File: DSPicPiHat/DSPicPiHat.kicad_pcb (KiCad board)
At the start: 2 copper layers, 65 x 66.5 mm, 87 parts, among them J10 Nice!View, J4 Conn_PIC_ICSP_ICD, J5 USB_C_Receptacle_USB2.0, J6 PowerInput, J7 GenericSPIconn, J8 RasPiHeaders, J9 GeneralSPIDisplay, SW1 POWER_Select, SW2 SW_DIP_x08, U1 DSPIC33CH512MP508T-I_PT, U10 DF5A6.2CJE_LM, U11 FT230XS, U12 NCP1117-3.3_SOT223, U2 ISO1640BDR, U3 DF5A6.2CJE_LM, U4 DF5A6.2CJE_LM, U5 ISO1640BDR, U6 DF5A6.2CJE_LM, U7 DF5A6.2CJE_LM, U8 ISO1640BDR, U9 DF5A6.2CJE_LM

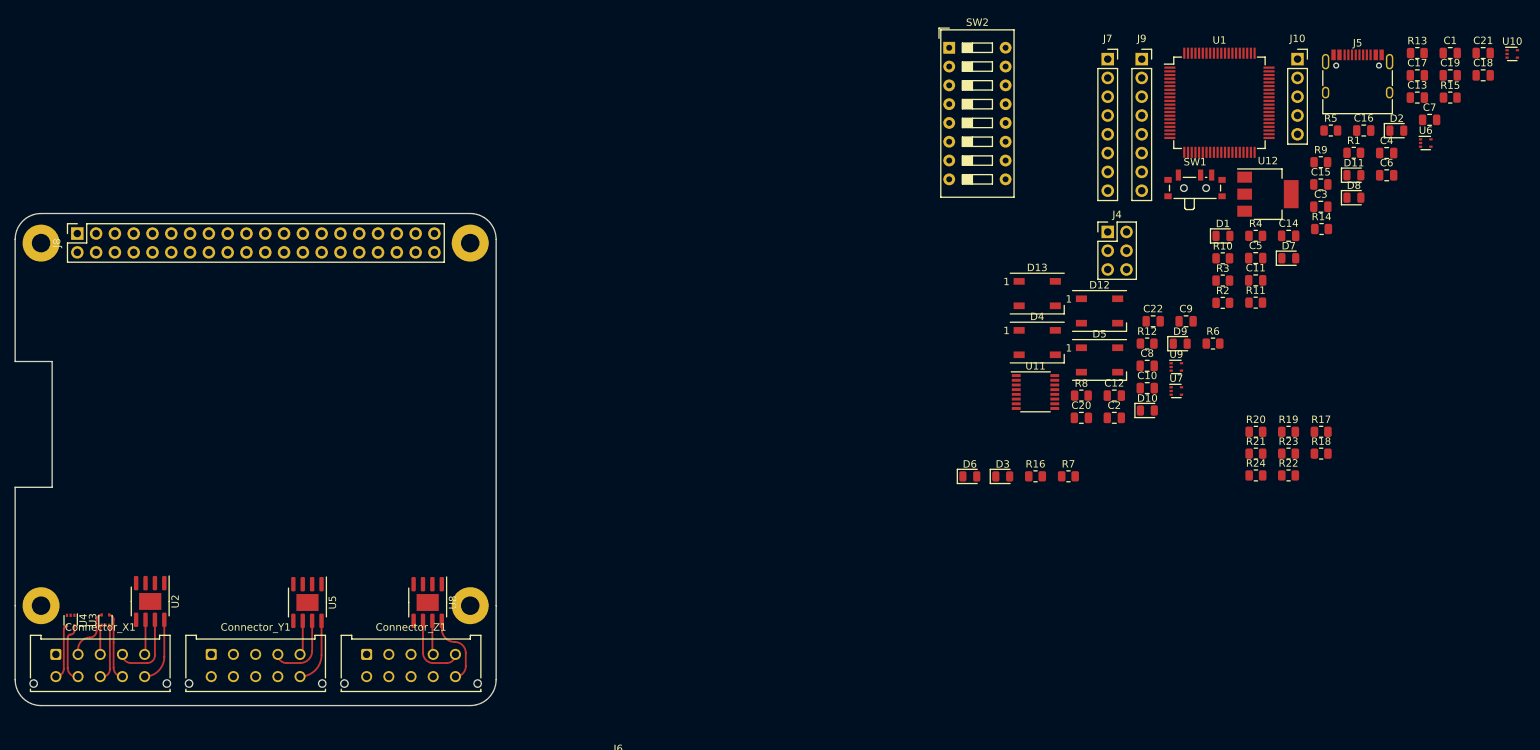
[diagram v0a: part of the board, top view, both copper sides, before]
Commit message: ESD connected to axis connectors.
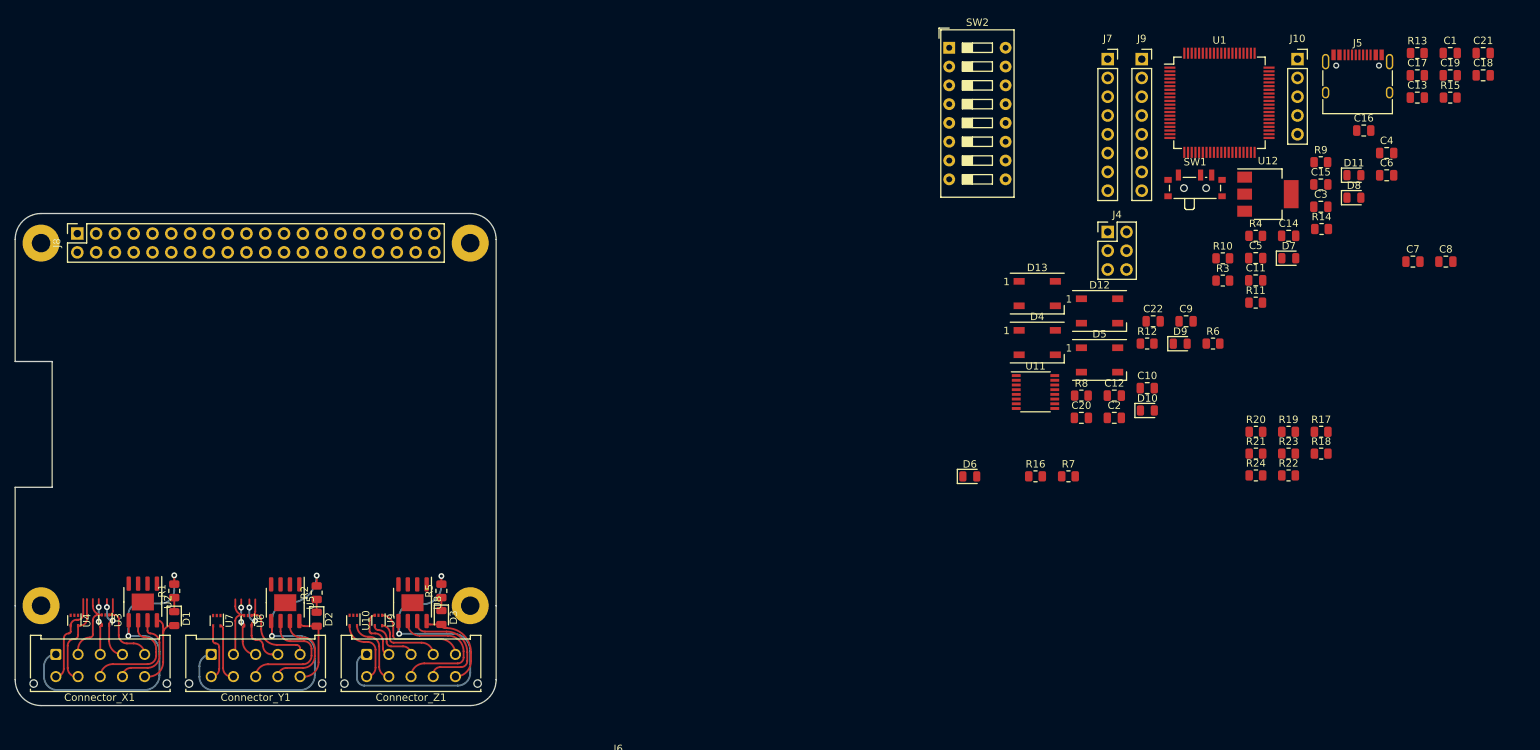
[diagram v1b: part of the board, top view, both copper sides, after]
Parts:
- moved U10 174.3 mm to (102.2, 128.5), turned to -90 degrees
- moved U6 171.8 mm to (88.0, 128.5), turned to -90 degrees
- moved R1 170.0 mm to (78.0, 124.5), turned to 90 degrees
- moved D2 160.2 mm to (97.2, 128.3), turned to -90 degrees
- moved D1 150.9 mm to (78.0, 128.2), turned to -90 degrees
- moved R5 135.3 mm to (114.1, 124.5), turned to 90 degrees
- moved U7 133.3 mm to (83.8, 128.5), turned to -90 degrees
- moved R2 128.6 mm to (97.2, 124.7), turned to 90 degrees
- moved U9 113.1 mm to (105.6, 128.5), turned to -90 degrees
- moved D3 78.2 mm to (114.1, 128.1), turned to -90 degrees
- moved C8 42.8 mm to (249.8, 80.0)
- moved C7 19.3 mm to (245.4, 80.0)
- moved U5 3.00 mm to (93.0, 126.1)
- moved U8 2.05 mm to (110.2, 126.1)
- moved U2 1.00 mm to (73.8, 126.0)
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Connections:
- Connector_X1 pad 2: EXT_X_PWM_00 -> EXT_ADC_X_00
- Connector_X1 pad 3: EXT_X_PWM_01 -> EXT_ADC_X_01
- Connector_X1 pad 4: EXT_X_SDA -> EXT_ADC_X_02
- Connector_X1 pad 5: EXT_X_SCL -> EXT_ADC_X_03
- Connector_X1 pad 6: EXT_ADC_X_00 -> EXT_X_PWM_00
- Connector_X1 pad 7: EXT_ADC_X_01 -> EXT_X_PWM_01
- Connector_X1 pad 8: EXT_ADC_X_02 -> EXT_X_SCL
- Connector_X1 pad 9: EXT_ADC_X_03 -> EXT_X_SDA
- Connector_Y1 pad 1: GNDY -> GNDZ
- Connector_Y1 pad 2: EXT_Y_PWM_00 -> EXT_ADC_Y_00
- Connector_Y1 pad 3: EXT_Y_PWM_01 -> EXT_ADC_Y_01
- Connector_Y1 pad 4: EXT_Y_SDA -> EXT_ADC_Y_02
- Connector_Y1 pad 5: EXT_Y_SCL -> EXT_ADC_Y_03
- Connector_Y1 pad 6: EXT_ADC_Y_00 -> EXT_Y_PWM_00
- Connector_Y1 pad 7: EXT_ADC_Y_01 -> EXT_Y_PWM_01
- Connector_Y1 pad 8: EXT_ADC_Y_02 -> EXT_Y_SCL
- Connector_Y1 pad 9: EXT_ADC_Y_03 -> EXT_Y_SDA
- Connector_Z1 pad 2: EXT_Z_PWM_00 -> EXT_ADC_Z_00
- Connector_Z1 pad 3: EXT_Z_PWM_01 -> EXT_ADC_Z_01
- Connector_Z1 pad 4: EXT_Z_SDA -> EXT_ADC_Z_02
- Connector_Z1 pad 5: EXT_Z_SCL -> EXT_ADC_Z_03
- Connector_Z1 pad 6: EXT_ADC_Z_00 -> EXT_Z_PWM_00
- Connector_Z1 pad 7: EXT_ADC_Z_01 -> EXT_Z_PWM_01
- Connector_Z1 pad 8: EXT_ADC_Z_02 -> EXT_Z_SCL
- Connector_Z1 pad 9: EXT_ADC_Z_03 -> EXT_Z_SDA
- U10 pad 3: EXT_Z_PWM_01 -> unconnected-(U10-Pad3)
- U10 pad 4: unconnected-(U10-Pad4) -> EXT_Z_PWM_00
- U10 pad 5: unconnected-(U10-Pad5) -> EXT_Z_PWM_01
- U3 pad 1: EXT_X_PWM_01 -> EXT_ADC_X_03
- U3 pad 3: EXT_ADC_X_02 -> EXT_ADC_X_00
- U3 pad 4: EXT_ADC_X_03 -> EXT_ADC_X_01
- U3 pad 5: EXT_X_PWM_00 -> EXT_ADC_X_02
- U4 pad 4: EXT_ADC_X_00 -> EXT_X_PWM_00
- U4 pad 5: EXT_ADC_X_01 -> EXT_X_PWM_01
- U5 pad 5: GNDY -> GNDZ
- U6 pad 3: EXT_ADC_Y_01 -> EXT_ADC_Y_00
- U6 pad 4: EXT_ADC_Y_00 -> EXT_ADC_Y_01
- U7 pad 3: EXT_Y_PWM_01 -> unconnected-(U7-Pad3)
- U7 pad 5: unconnected-(U7-Pad5) -> EXT_Y_PWM_01
- U9 pad 1: EXT_ADC_Z_02 -> EXT_ADC_Z_03
- U9 pad 3: EXT_ADC_Z_01 -> EXT_ADC_Z_00
- U9 pad 4: EXT_ADC_Z_00 -> EXT_ADC_Z_01
- U9 pad 5: EXT_ADC_Z_03 -> EXT_ADC_Z_02
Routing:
- net GNDZ: track 0.00 -> 141.3 mm, vias 0 -> 6
- net EXT_ADC_Z_03: track 0.00 -> 13.3 mm
- net EXT_ADC_Y_03: track 0.00 -> 12.7 mm
- net EXT_Y_SCL: track 4.73 -> 16.8 mm
- net EXT_Z_SDA: track 4.57 -> 16.2 mm
- net EXT_ADC_Y_02: track 0.00 -> 10.4 mm, vias 0 -> 1
- net EXT_X_SCL: track 4.74 -> 15.1 mm
- net EXT_ADC_Y_00: track 0.00 -> 9.74 mm
- net EXT_Z_PWM_00: track 0.00 -> 9.59 mm
- net EXT_ADC_Z_02: track 0.00 -> 9.31 mm
- net EXT_Z_PWM_01: track 0.00 -> 9.26 mm
- net EXT_Z_SCL: track 10.1 -> 19.2 mm
- net EXT_X_PWM_01: track 4.04 -> 12.8 mm
- net EXT_ADC_Y_01: track 0.00 -> 8.69 mm, vias 0 -> 2
- net EXT_Y_PWM_01: track 0.00 -> 7.91 mm
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
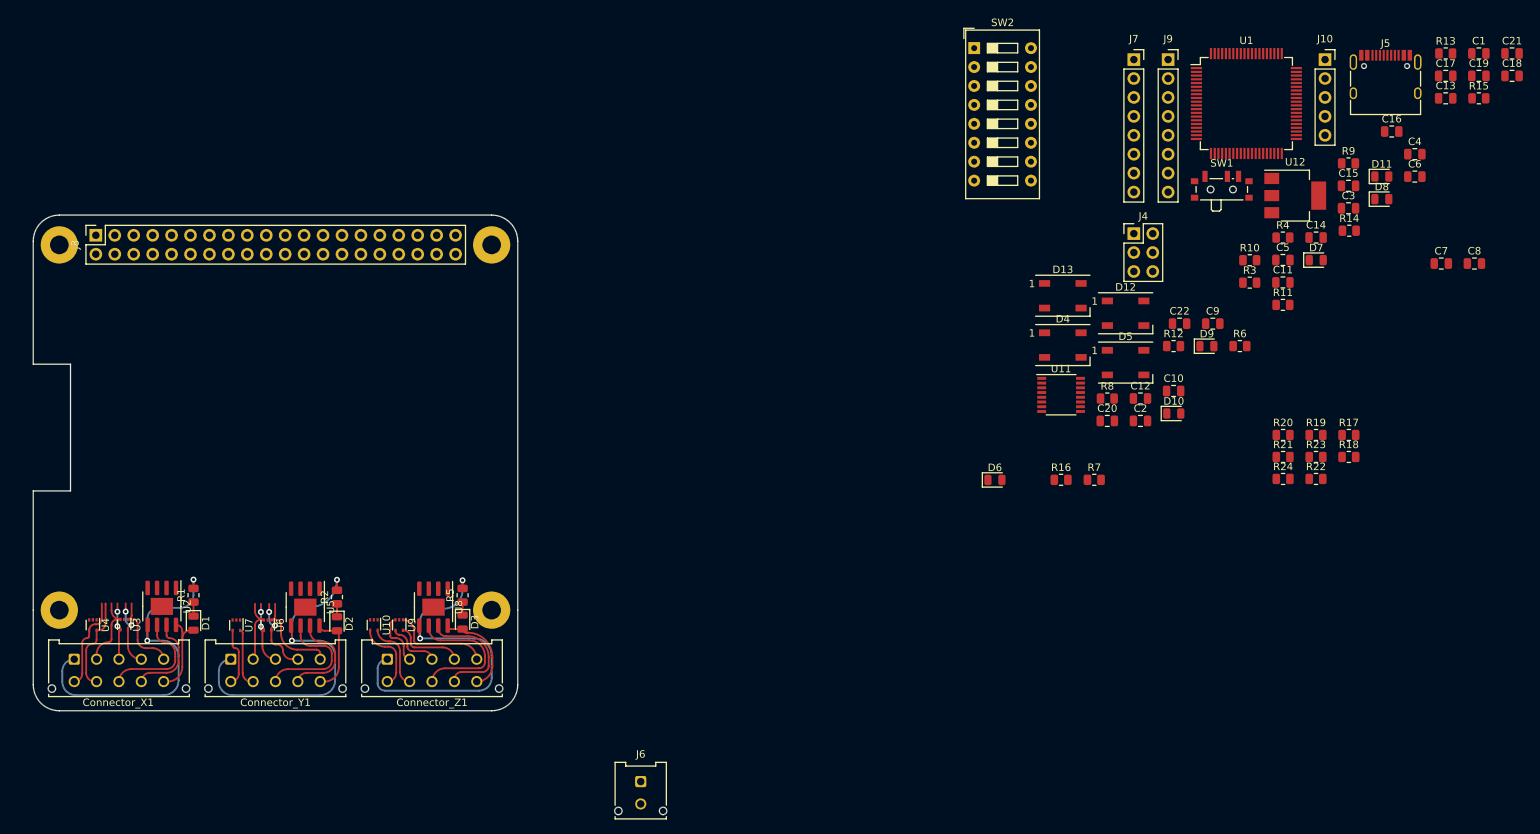
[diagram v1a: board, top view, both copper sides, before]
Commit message: Connected all the coil driver connectors. Added more footprints.
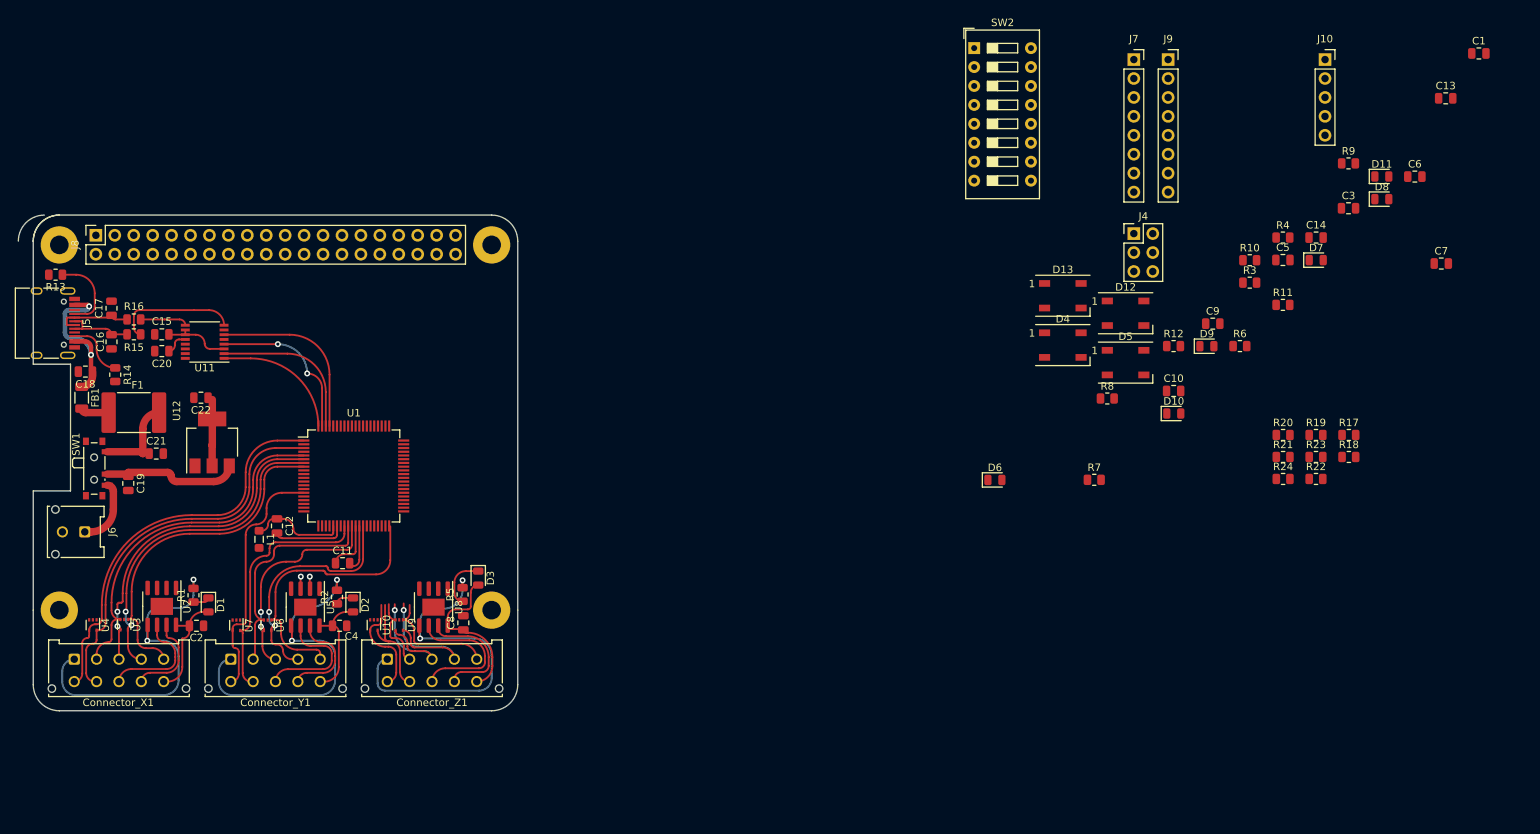
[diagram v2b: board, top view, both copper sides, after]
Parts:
- added F1: 3.5 A(?), Fuse:Fuse_2920_7451Metric, F.Cu at (70.0, 100.0)
- added FB1: FerriteBead_Small, Resistor_SMD:R_1206_3216Metric, F.Cu at (63.0, 98.0)
- added L1: 10 mA <1o, Inductor_SMD:L_0805_2012Metric_Pad1.05x1.20mm_HandSolder, F.Cu at (86.8, 117.0)
- moved C18 195.5 mm to (63.5, 94.5), turned to 180 degrees
- moved C21 189.7 mm to (73.0, 105.5)
- moved C19 189.3 mm to (69.2, 109.5), turned to -90 degrees
- moved R13 188.8 mm to (59.5, 81.5), turned to 180 degrees
- moved R15 183.2 mm to (70.0, 89.5)
- moved J5 182.7 mm to (58.0, 88.0), turned to -90 degrees
- moved C17 181.7 mm to (67.0, 86.0), turned to 90 degrees
- moved C16 174.1 mm to (67.0, 90.5), turned to -90 degrees
- moved R14 166.7 mm to (67.5, 94.9), turned to -90 degrees
- moved C15 160.4 mm to (73.8, 89.5), turned to 180 degrees
- moved C4 157.5 mm to (97.6, 128.6)
- moved SW1 155.6 mm to (65.0, 107.5), turned to -90 degrees
- moved U12 149.0 mm to (80.5, 104.0), turned to 90 degrees
- moved C8 144.0 mm to (114.2, 128.2), turned to 90 degrees
- moved C22 131.7 mm to (79.0, 98.0), turned to 180 degrees
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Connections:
- U1 pad 15: EXT_ADC_X_03 -> EXT_Y_PWM_00
- U1 pad 28: unconnected-(U1-Pad28) -> EXT_Y_PWM_01
- U1 pad 29: unconnected-(U1-Pad29) -> EXT_ADC_Y_00
- U1 pad 3: EXT_Y_PWM_00 -> EXT_X_PWM_01
- U1 pad 30: unconnected-(U1-Pad30) -> EXT_ADC_Y_01
- U1 pad 33: unconnected-(U1-Pad33) -> EXT_ADC_Y_02
- U1 pad 40: unconnected-(U1-Pad40) -> EXT_ADC_Y_03
- U1 pad 41: EXT_ADC_Y_00 -> unconnected-(U1-Pad41)
- U1 pad 43: EXT_ADC_Y_01 -> unconnected-(U1-Pad43)
- U1 pad 45: EXT_ADC_Y_02 -> unconnected-(U1-Pad45)
- U1 pad 46: EXT_ADC_Y_03 -> unconnected-(U1-Pad46)
- U1 pad 5: EXT_Z_PWM_00 -> EXT_ADC_X_00
- U1 pad 6: EXT_ADC_X_00 -> EXT_ADC_X_01
- U1 pad 64: unconnected-(U1-Pad64) -> EXT_Z_PWM_01
- U1 pad 7: EXT_ADC_X_01 -> EXT_ADC_X_02
- U1 pad 72: EXT_Z_PWM_01 -> unconnected-(U1-Pad72)
- U1 pad 73: EXT_Y_PWM_01 -> unconnected-(U1-Pad73)
- U1 pad 74: EXT_X_PWM_01 -> EXT_Z_PWM_00
- U1 pad 8: EXT_ADC_X_02 -> EXT_ADC_X_03
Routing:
- net EXT_X_PWM_00: track 12.5 -> 52.1 mm
- net EXT_X_PWM_01: track 12.8 -> 51.2 mm
- net EXT_ADC_X_00: track 10.0 -> 46.9 mm
- net EXT_ADC_X_01: track 7.81 -> 44.1 mm
- net EXT_ADC_X_02: track 9.11 -> 44.2 mm, vias 3 -> 2
- net EXT_ADC_X_03: track 11.1 -> 45.2 mm
- net EXT_Y_PWM_01: track 7.91 -> 33.3 mm
- net EXT_Y_PWM_00: track 7.88 -> 33.2 mm
- net EXT_ADC_Y_03: track 12.7 -> 37.3 mm
- net U1CTS: track 0.00 -> 23.9 mm
- net Net-(C18-Pad1): track 0.00 -> 22.2 mm, vias 0 -> 2
- net U1RX: track 0.00 -> 21.6 mm, vias 0 -> 2
- net EXT_ADC_Y_02: track 10.4 -> 31.8 mm, vias 1 -> 2
- net EXT_ADC_Y_00: track 9.74 -> 31.0 mm
- net U1RTS: track 0.00 -> 20.9 mm
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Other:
- board size 65 x 66.5 mm -> 67 x 66.5 mm
